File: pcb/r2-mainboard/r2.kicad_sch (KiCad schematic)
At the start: 0 parts

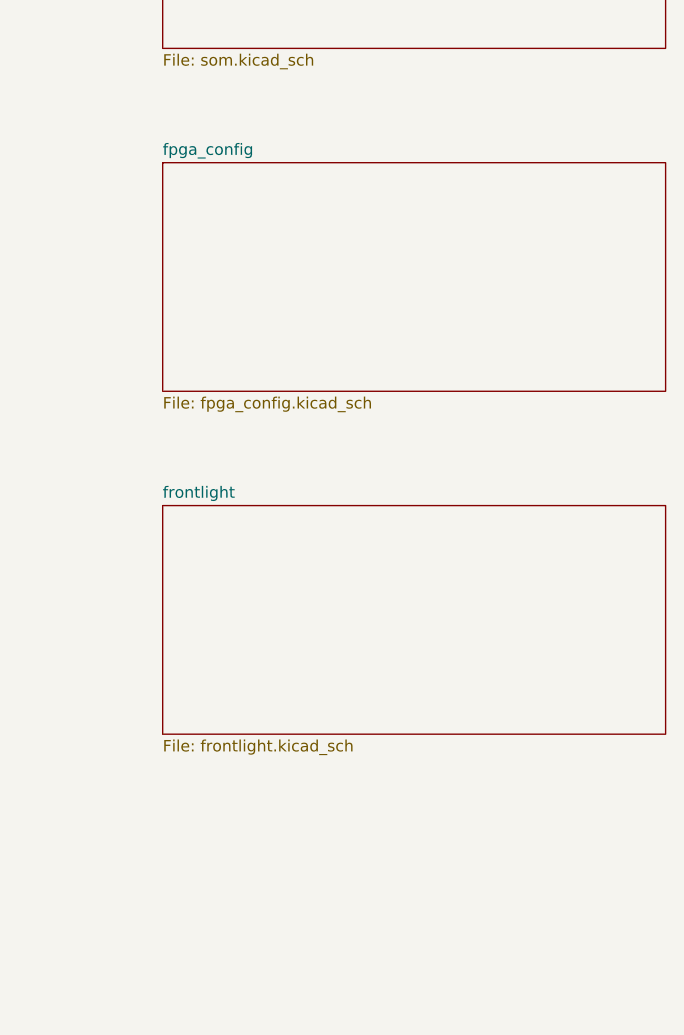
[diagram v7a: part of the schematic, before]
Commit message: R2: WP5 -- fpga_config ported (bank 2, config pins, clock, JTAG)
Units 3 and 5 of the XC6SLX16: bank 2's I/O, the dedicated configuration pins,
the 33.33 MHz oscillator and the JTAG group. Ported by tools/port_r1.py; the new
content this sheet needs (config NOR, the M1 strap change, the debug header, an
INIT_B pull-up) is NOT here yet and comes next.

A STALE RAIL, CAUGHT BY THE NETLIST DIFF
R1 spreads the FPGA's decoupling across sheets, so five of the DDR bank's VCCO
capacitors are drawn on fpga_config rather than fpga_ddr. They ported across as
`+1V35` -- the name retired in 8b69e01 when the bank moved to 1.5 V. ERC was
silent about it; the netlist diff showed a new 5-node +1V35 net appearing out of
nowhere. Fixed through RAILS, and +1V5 now carries C316/C448/C457/C485/C489
alongside the existing power_mon shunt. fpga_ddr carries the same name in five
places and will need the same treatment.

That is the third time this session that a netlist node-diff caught something
ERC did not: the U11 deletion, the fpga_io cross-sheet short, and now this.

R1 LEAVES INIT_B UNCONNECTED
FPGA_INIT is a *local* label on R1 whose net has exactly one member, U41.R3 --
no pull-up, no route anywhere. The HIER mapping assumed it was a sheet-level
signal and the tool's own guard rejected it, which is how it came to light. It
stays local through the port so the sheet matches R1, but it matters more in R2
than in R1: with self-boot, INIT_B low is how firmware tells a CRC error from
"still configuring" when DONE never arrives. Giving it a pull-up and a route to
the MCU is a separate change.

THE 14 LVDS BALLS ARE DROPPED
R2 deletes the PTN3460 that drove the FPD-Link input, so those balls have no
source. Left as constrained-but-floating LVDS_33 inputs with DIFF_TERM enabled,
seven differential buffers would sit at an indeterminate common mode where they
can self-oscillate and draw current -- in the reading state, the one number R2
exists to reduce. The owner's decision (2026-08-12) is to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
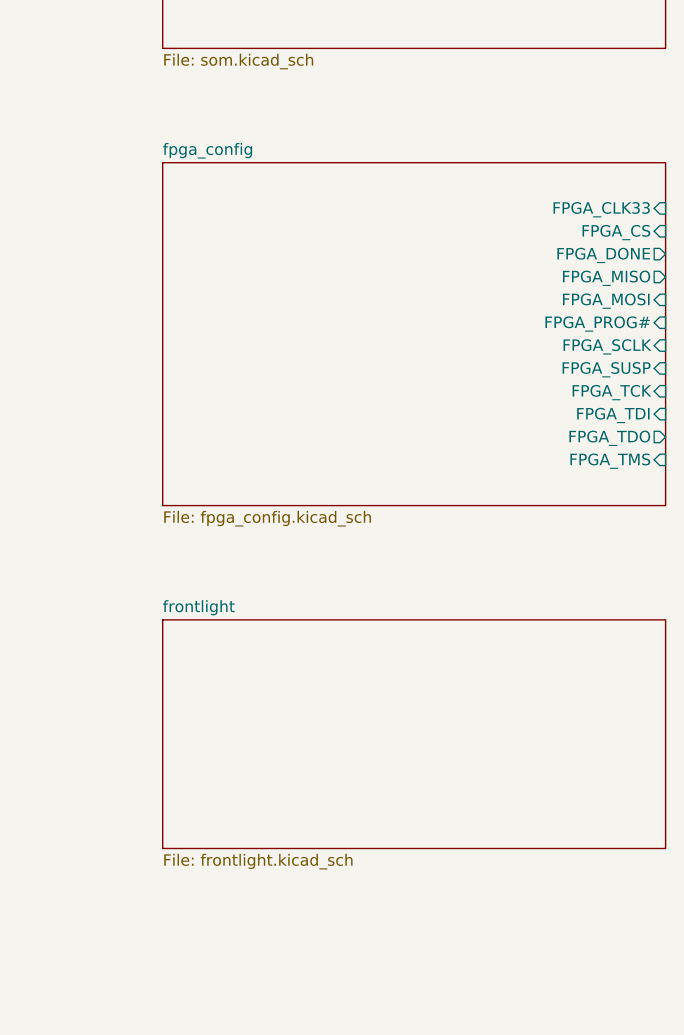
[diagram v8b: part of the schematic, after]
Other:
- sheet fpga_config ports: added FPGA_CLK33, FPGA_CS, FPGA_DONE, FPGA_MISO, FPGA_MOSI, FPGA_PROG#, FPGA_SCLK, FPGA_SUSP, FPGA_TCK, FPGA_TDI, FPGA_TDO, FPGA_TMS; removed none
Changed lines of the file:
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@@
 	)
 	(sheet
-		(at 320.04 106.68)
+		(at 320.04 119.38)
 		(size 55.88 25.4)
 		(exclude_from_sim no)
@@
 		)
 		(property "Sheetname" "frontlight"
-			(at 320.04 105.9674 0)
+			(at 320.04 118.6674 0)
 			(show_name no)
 			(do_not_autoplace no)
@@
 		)
 		(property "Sheetfile" "frontlight.kicad_sch"
-			(at 320.04 132.6646 0)
+			(at 320.04 145.3646 0)
 			(show_name no)
 			(do_not_autoplace no)
@@
 	(sheet
 		(at 320.04 68.58)
-		(size 55.88 25.4)
+		(size 55.88 38.1)
 		(exclude_from_sim no)
 		(in_bom yes)
@@
 		)
 		(property "Sheetfile" "fpga_config.kicad_sch"
-			(at 320.04 94.5646 0)
+			(at 320.04 107.2646 0)
 			(show_name no)
 			(do_not_autoplace no)
@@
 			)
 		)
+		(pin "FPGA_CLK33" input
+			(at 375.92 73.66 0)
+			(effects
+				(font
+					(size 1.27 1.27)
+				)
+				(justify right)
+			)
+		)
+		(pin "FPGA_CS" input
+			(at 375.92 76.2 0)
+			(effects
+				(font
+					(size 1.27 1.27)
+				)
+				(justify right)
+			)
+		)
+		(pin "FPGA_DONE" output
+			(at 375.92 78.74 0)
+			(effects
+				(font
+					(size 1.27 1.27)
+				)
+				(justify right)
+			)
+		)
+		(pin "FPGA_MISO" output
+			(at 375.92 81.28 0)
+			(effects
+				(font
+					(size 1.27 1.27)
+				)
+				(justify right)
+			)
+		)
+		(pin "FPGA_MOSI" input
+			(at 375.92 83.82 0)
+			(effects
+				(font
+					(size 1.27 1.27)
+				)
+				(justify right)
+			)
+		)
+		(pin "FPGA_PROG#" input
+			(at 375.92 86.36 0)
+			(effects
+				(font
+					(size 1.27 1.27)
+				)
+				(justify right)
+			)
+		)
+		(pin "FPGA_SCLK" input
+			(at 375.92 88.9 0)
+			(effects
+				(font
+					(size 1.27 1.27)
+				)
+				(justify right)
+			)
+		)
+		(pin "FPGA_SUSP" input
+			(at 375.92 91.44 0)
+			(effects
+				(font
+					(size 1.27 1.27)
+				)
+				(justify right)
+			)
+		)
+		(pin "FPGA_TCK" input
+			(at 375.92 93.98 0)
+			(effects
+				(font
+					(size 1.27 1.27)
+				)
+				(justify right)
+			)
+		)
+		(pin "FPGA_TDI" input
+			(at 375.92 96.52 0)
+			(effects
+				(font
+					(size 1.27 1.27)
+				)
+				(justify right)
+			)
+		)
+		(pin "FPGA_TDO" output
+			(at 375.92 99.06 0)
+			(effects
+				(font
+					(size 1.27 1.27)
+				)
+				(justify right)
+			)
+		)
+		(pin "FPGA_TMS" input
+			(at 375.92 101.6 0)
+			(effects
+				(font
+					(size 1.27 1.27)
+				)
+				(justify right)
+			)
+		)
